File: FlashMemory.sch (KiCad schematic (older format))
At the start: 3 parts, among them U11 IS25LP256D-xM, U6 W25QxxJVS

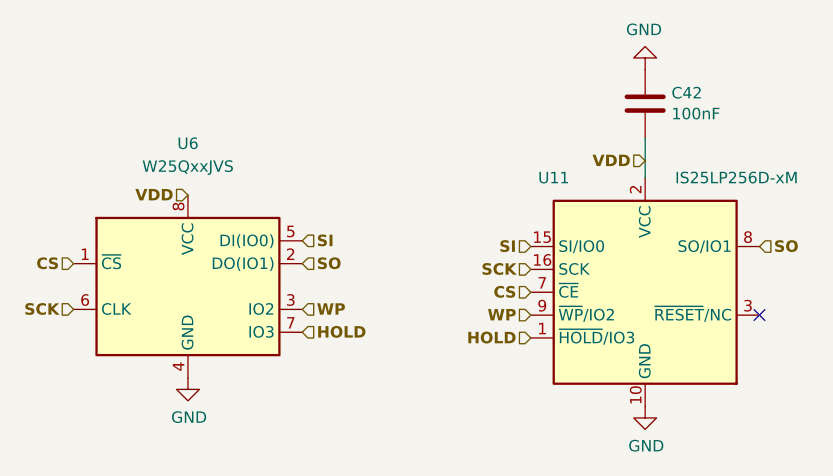
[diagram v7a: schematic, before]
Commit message: changed U6 description per the below https://github.com/rusefi/hw_microRusEfi/issues/169
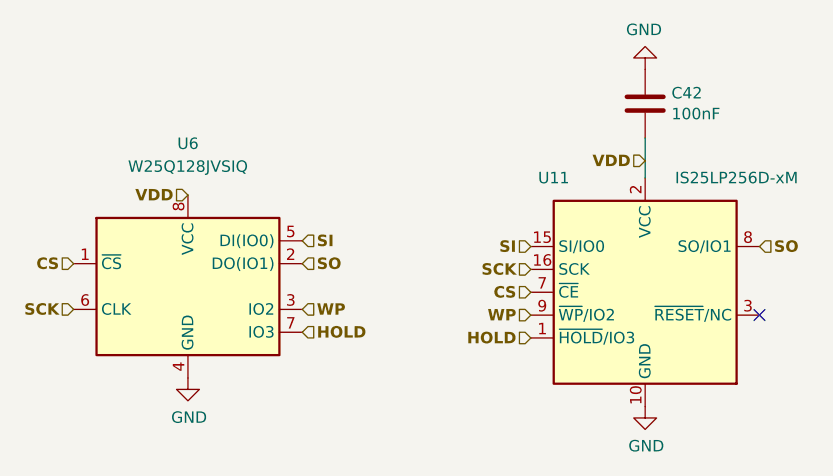
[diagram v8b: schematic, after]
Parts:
- U6: value W25QxxJVS -> W25Q128JVSIQ
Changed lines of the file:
@@
 P 4000 2725
 F 0 "U6" H 4000 3350 50  0000 C CNN
-F 1 "W25QxxJVS" H 4000 3250 50  0000 C CNN
+F 1 "W25Q128JVSIQ " H 4000 3250 50  0000 C CNN
 F 2 "hw_microRusEfi-master:SO-8_5.3x6.2mm_P1.27mm-150+208" H 4000 2725 50  0001 C CNN
 F 3 "http://www.winbond.com/resource-files/w25q32jv%20revg%2003272018%20plus.pdf" H 4000 2725 50  0001 C CNN
